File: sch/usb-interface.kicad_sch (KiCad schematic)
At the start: 0 parts

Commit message: annotation
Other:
- company: (none) -> NTNU, NINA
- title: (none) -> USB Interface
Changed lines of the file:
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@@
 	(generator_version "9.0")
 	(paper "A4")
+	(title_block
+		(title "USB Interface")
+		(date "2026-01-29")
+		(rev "0")
+		(company "NTNU, NINA")
+		(comment 1 "https://github.com/oveljosland/audiograb-pcb/")
+		(comment 2 "GNU Affero General Public Licence Version 3")
+	)
 )

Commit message: Added SD_USB interface unit and USB_hub unit
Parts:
- added IC1: USB2244I-AEZG-06, QFN50P600X600X90-37N-D, symbol USB2244I-AEZG-06:USB2244I-AEZG-06
- added U1: USB2514B_Bi, Package_DFN_QFN:QFN-36-1EP_6x6mm_P0.5mm_EP3.7x3.7mm, symbol Interface_USB:USB2514B_Bi

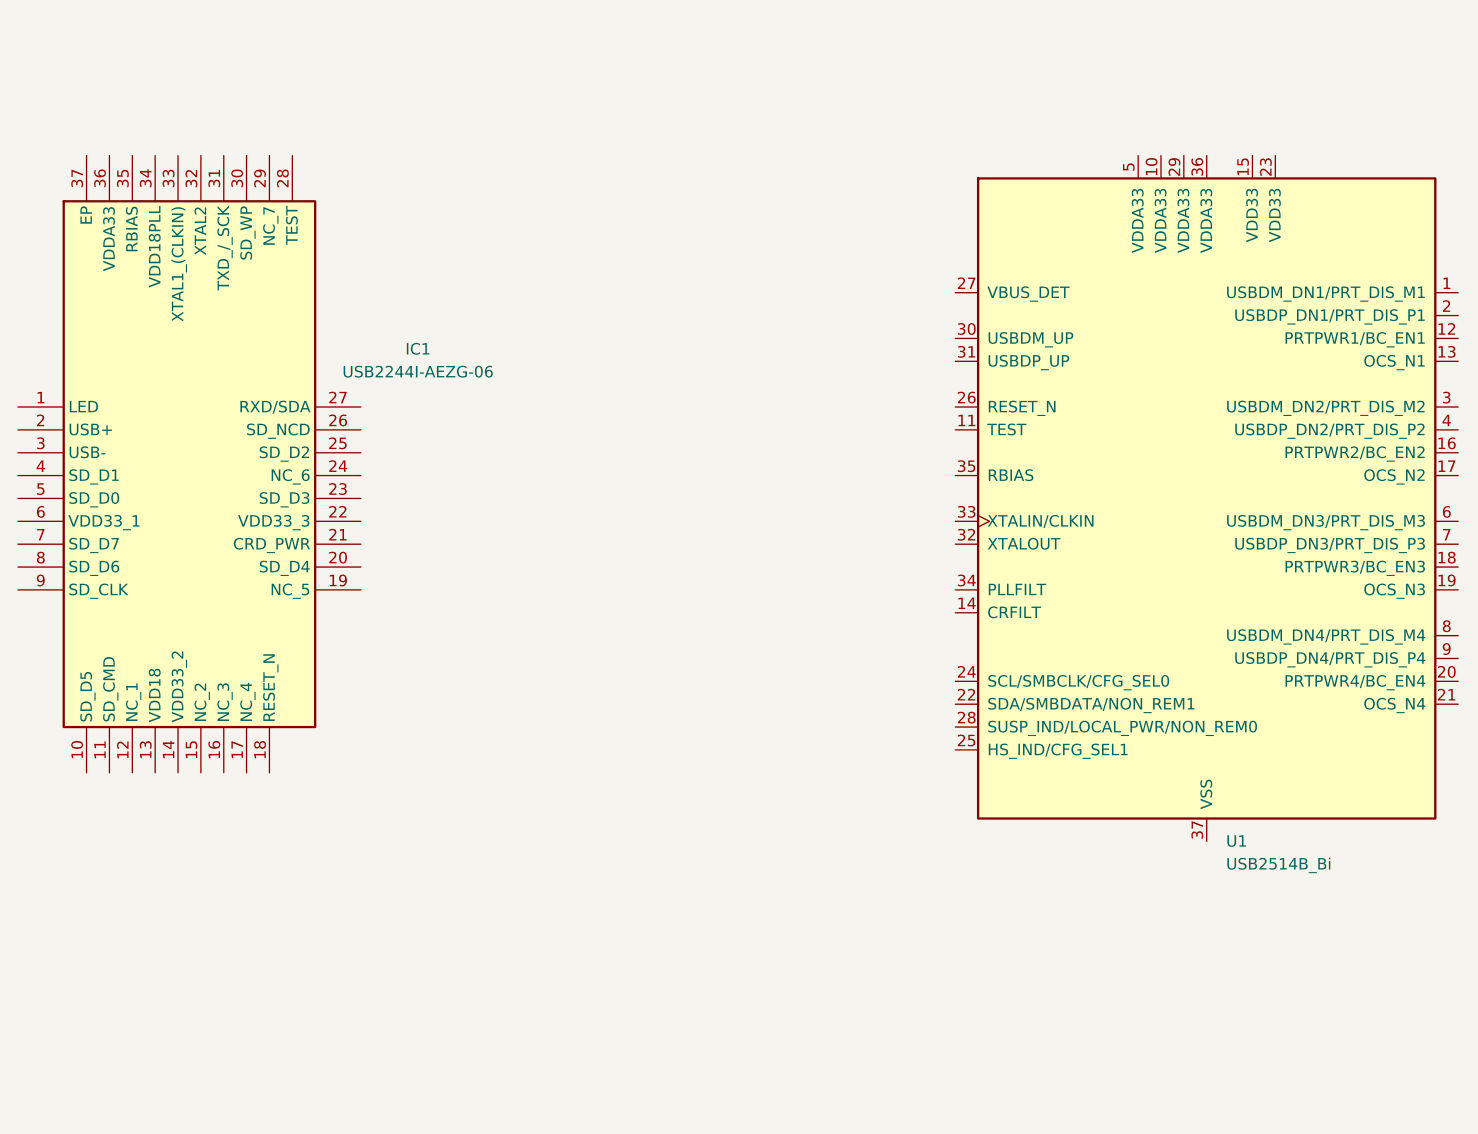
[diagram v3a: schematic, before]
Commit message: Added most pins that interact with other schematics
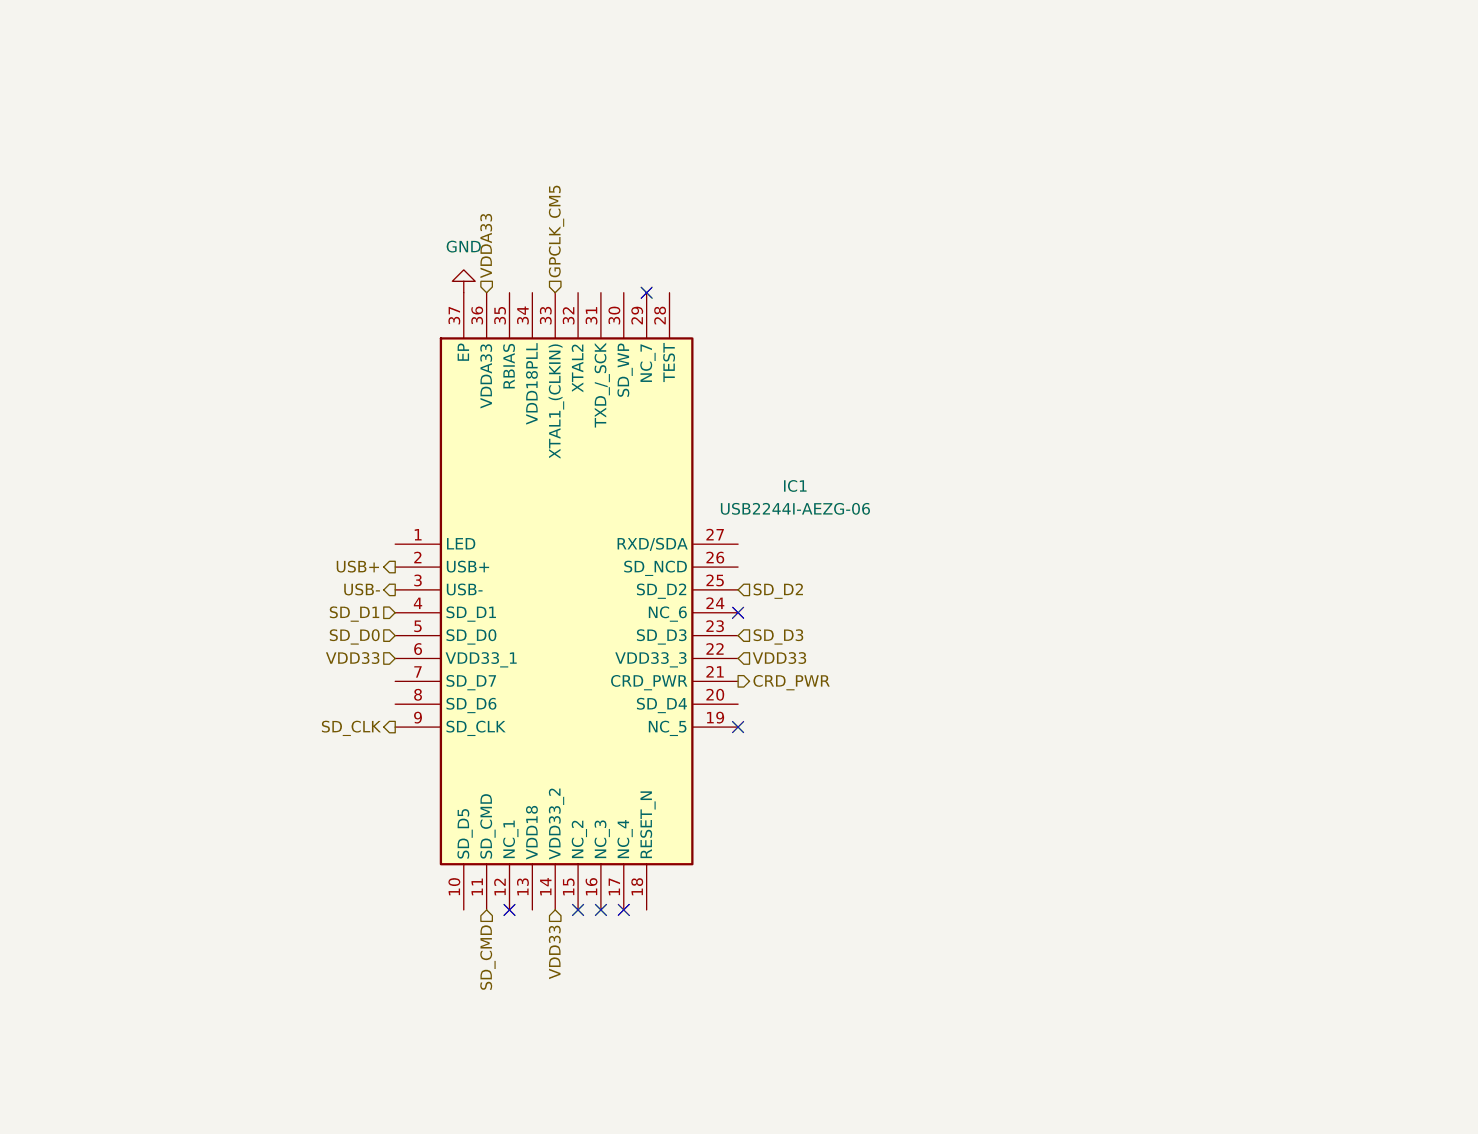
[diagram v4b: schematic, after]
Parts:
- removed U1: USB2514B_Bi, Package_DFN_QFN:QFN-36-1EP_6x6mm_P0.5mm_EP3.7x3.7mm, symbol Interface_USB:USB2514B_Bi
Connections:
- net SD_CMD: now reaches IC1.11 (SD_CMD)
- net VDD33: now reaches IC1.14 (VDD33_2)
- net VDD33: now also IC1.22 (VDD33_3), IC1.6 (VDD33_1)
- net USB+: now reaches IC1.2 (USB+)
- net CRD_PWR: now reaches IC1.21 (CRD_PWR)
- net SD_D3: now reaches IC1.23 (SD_D3)
- net SD_D2: now reaches IC1.25 (SD_D2)
- net USB-: now reaches IC1.3 (USB-)
- net GPCLK_CM5: now reaches IC1.33 (XTAL1_(CLKIN))
- net VDDA33: now reaches IC1.36 (VDDA33)
- net GND: now reaches IC1.37 (EP)
- net SD_D1: now reaches IC1.4 (SD_D1)
- net SD_D0: now reaches IC1.5 (SD_D0)
- net SD_CLK: now reaches IC1.9 (SD_CLK)
- no-connect marks 0 -> 7
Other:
- moved on the sheet: IC1

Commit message: All pins set
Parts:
- added C1, C2: 1.0 µ, symbol Device:C
- added R1: 12.0 k, symbol Device:R
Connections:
- net GND: now also IC1.28 (TEST), C1.1, C2.2, R1.1
- net at IC1.13 (VDD18): now also C2.1
- net RESET: now reaches IC1.18 (RESET_N)
- net at IC1.34 (VDD18PLL): now also C1.2
- net at IC1.35 (RBIAS): now also R1.2
- no-connect marks 7 -> 17
